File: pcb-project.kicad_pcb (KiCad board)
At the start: 2 copper layers, 110 x 60 mm, 62 parts, among them J1 Conn_01x03, J2 USB_C_Receptacle_USB2.0_16P, J3 Conn_01x14, J4 Conn_01x02, J5 Conn_01x05, J6 Conn_01x06, Q1 MMBT2222A, SW1 SW_Push, SW10 SW_Push, SW2 SW_Push, SW3 SW_Push, SW4 SW_Push, SW5 SW_Push, SW6 SW_Push, SW7 SW_Push, SW8 SW_Push, SW9 SW_Push, U1 RP2040, U2 W25Q128JVS, U3 AP2112K-3.3, U4 PAM8302AAD, Y1 12MHz

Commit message: Started arranging components, will continue tomorrow
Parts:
- moved J4 79.5 mm to (196.0, 104.0), turned to 0 degrees
- moved C17 61.4 mm to (174.5, 56.5), turned to 90 degrees
- moved C20 59.2 mm to (190.5, 92.5), turned to 0 degrees
- moved J5 54.2 mm to (112.0, 62.0), turned to 0 degrees
- moved C16 53.9 mm to (166.5, 56.5), turned to 90 degrees
- moved U4 49.2 mm to (186.0, 98.0), turned to 0 degrees
- moved U3 47.5 mm to (170.5, 56.5), turned to 0 degrees
- moved C23 45.9 mm to (179.5, 100.0), turned to 0 degrees
- moved C22 45.2 mm to (176.0, 100.0), turned to 0 degrees
- moved U2 42.9 mm to (169.0, 72.0)
- moved R13 42.6 mm to (179.5, 96.0), turned to 0 degrees
- moved R11 42.2 mm to (176.0, 96.0), turned to 0 degrees
- moved R12 41.9 mm to (176.0, 98.0), turned to 0 degrees
- moved C19 37.3 mm to (186.0, 92.5), turned to 0 degrees
- moved C21 31.9 mm to (179.5, 98.0), turned to 0 degrees
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
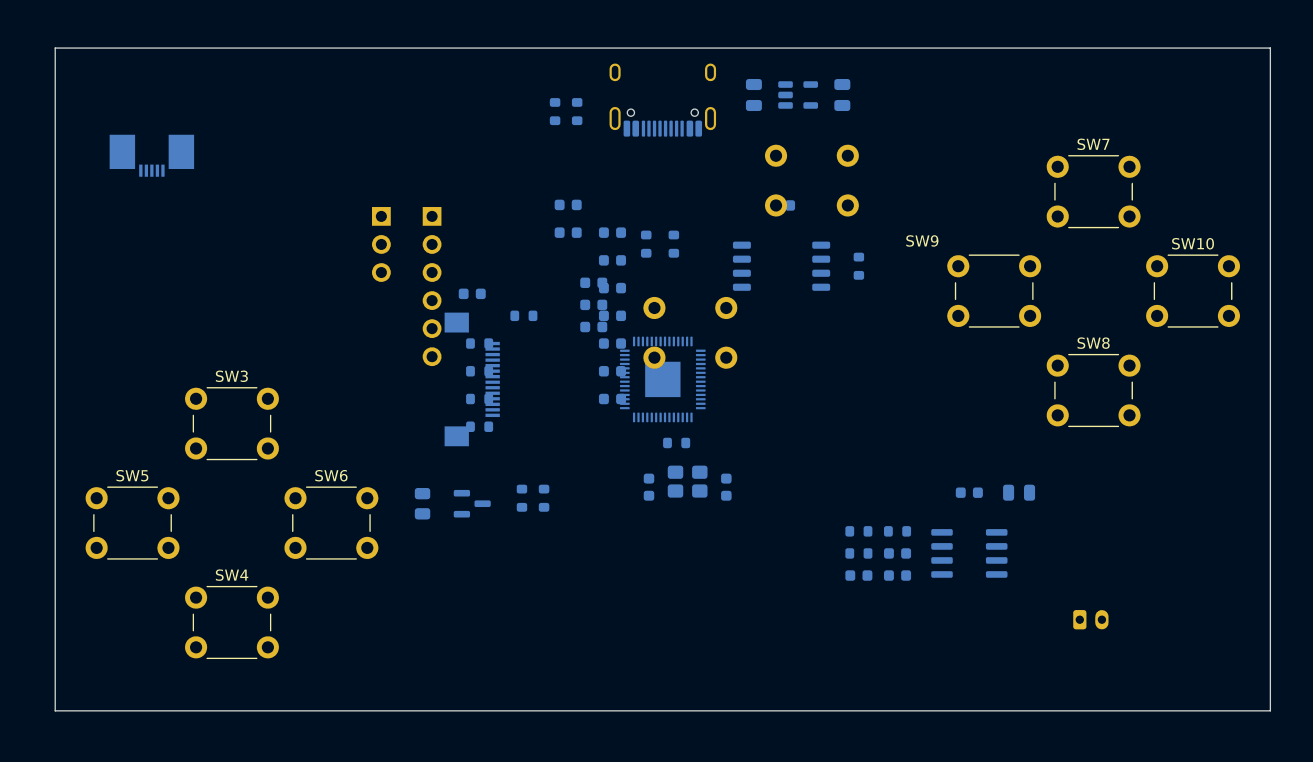
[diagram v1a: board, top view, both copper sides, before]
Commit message: Board outline and placement done
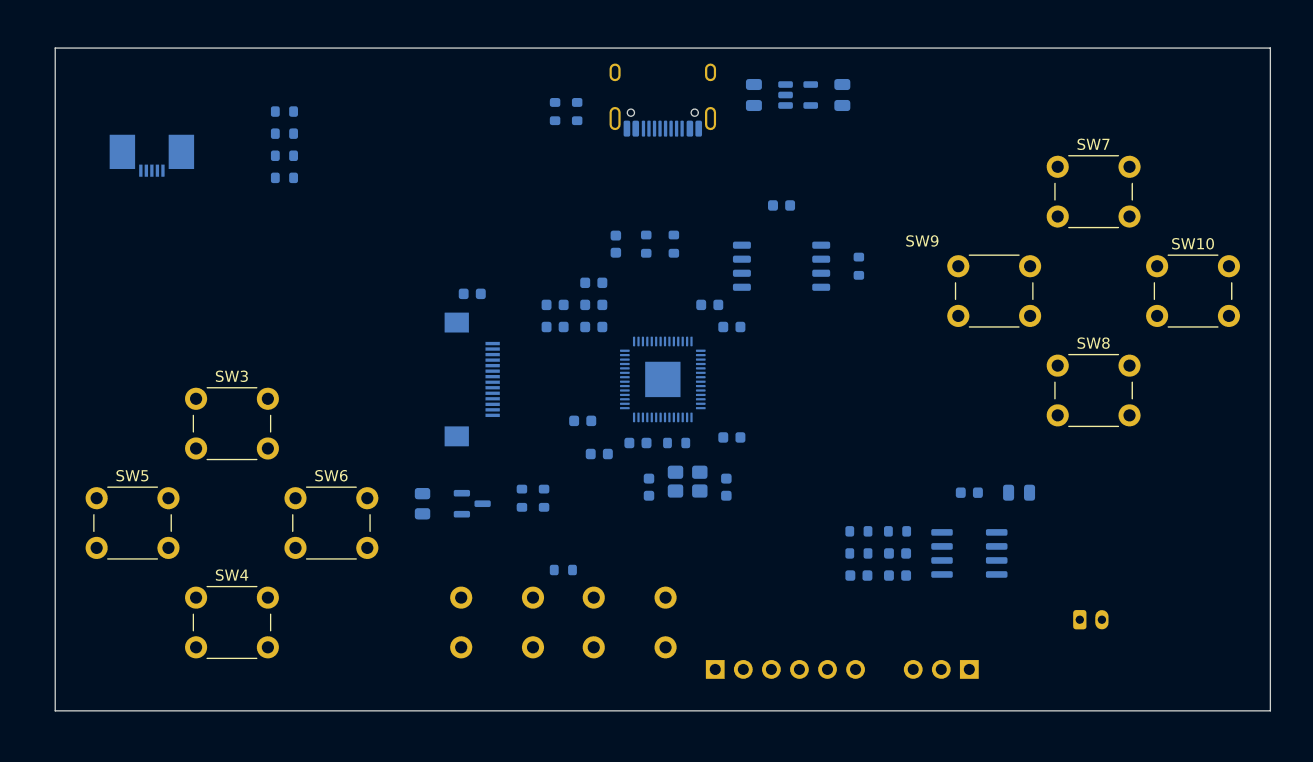
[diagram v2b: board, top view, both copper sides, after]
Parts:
- moved J1 67.2 mm to (186.0, 108.5), turned to 90 degrees
- moved SW1 56.6 mm to (140.0, 106.5), turned to 0 degrees
- moved J6 48.4 mm to (163.0, 108.5), turned to -90 degrees
- moved SW2 33.0 mm to (152.0, 106.5), turned to 0 degrees
- moved R18 28.6 mm to (124.0, 64.0), turned to 0 degrees
- moved R17 28.2 mm to (124.0, 62.0), turned to 0 degrees
- moved R15 27.8 mm to (124.0, 60.0), turned to 0 degrees
- moved R14 27.4 mm to (124.0, 58.0), turned to 0 degrees
- moved R3 23.3 mm to (149.2, 99.5), turned to 0 degrees
- moved C11 20.2 mm to (152.5, 89.0), turned to 0 degrees
- moved C4 17.3 mm to (164.5, 87.5), turned to 0 degrees
- moved C10 15.7 mm to (162.5, 75.5), turned to 0 degrees
- moved C2 13.8 mm to (164.5, 77.5), turned to 0 degrees
- moved C5 11.7 mm to (156.0, 88.0), turned to 0 degrees
- moved C8 9.98 mm to (148.5, 75.5), turned to 0 degrees
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
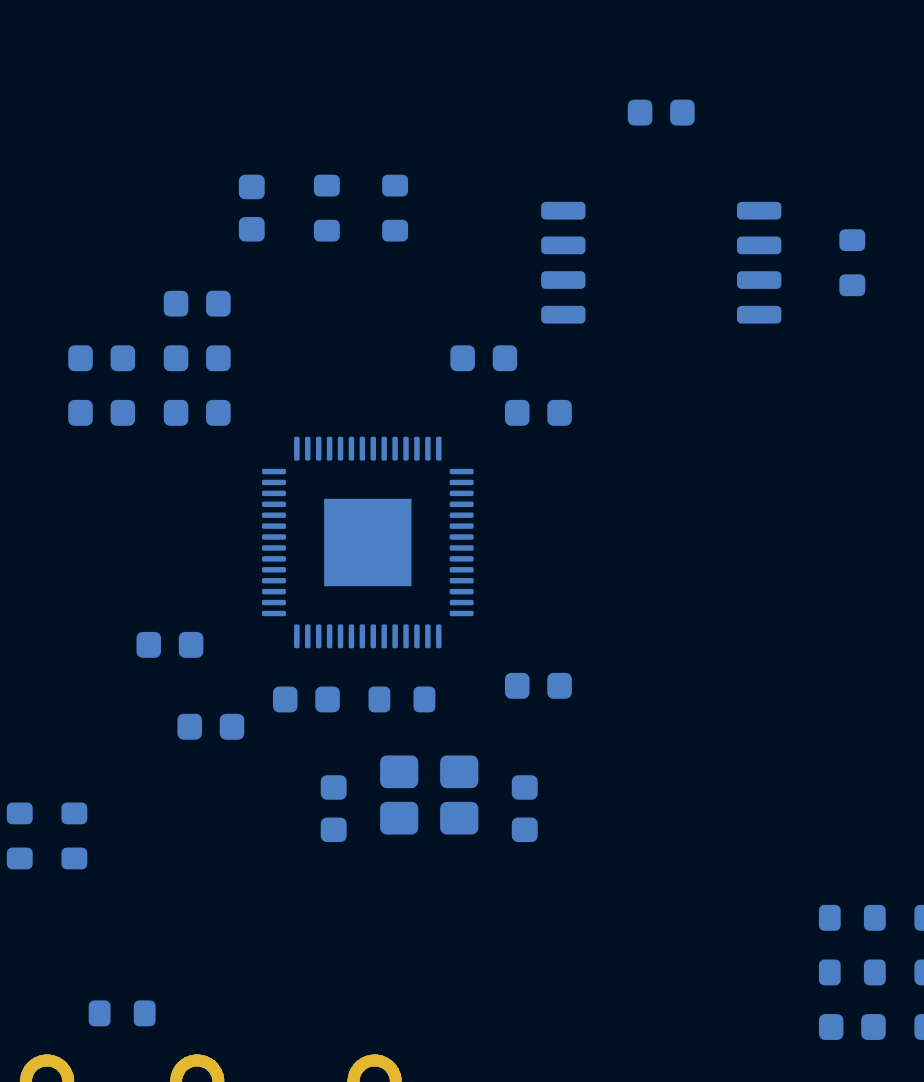
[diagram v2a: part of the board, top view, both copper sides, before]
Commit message: Crystal routed, RP2040 orientation fixed
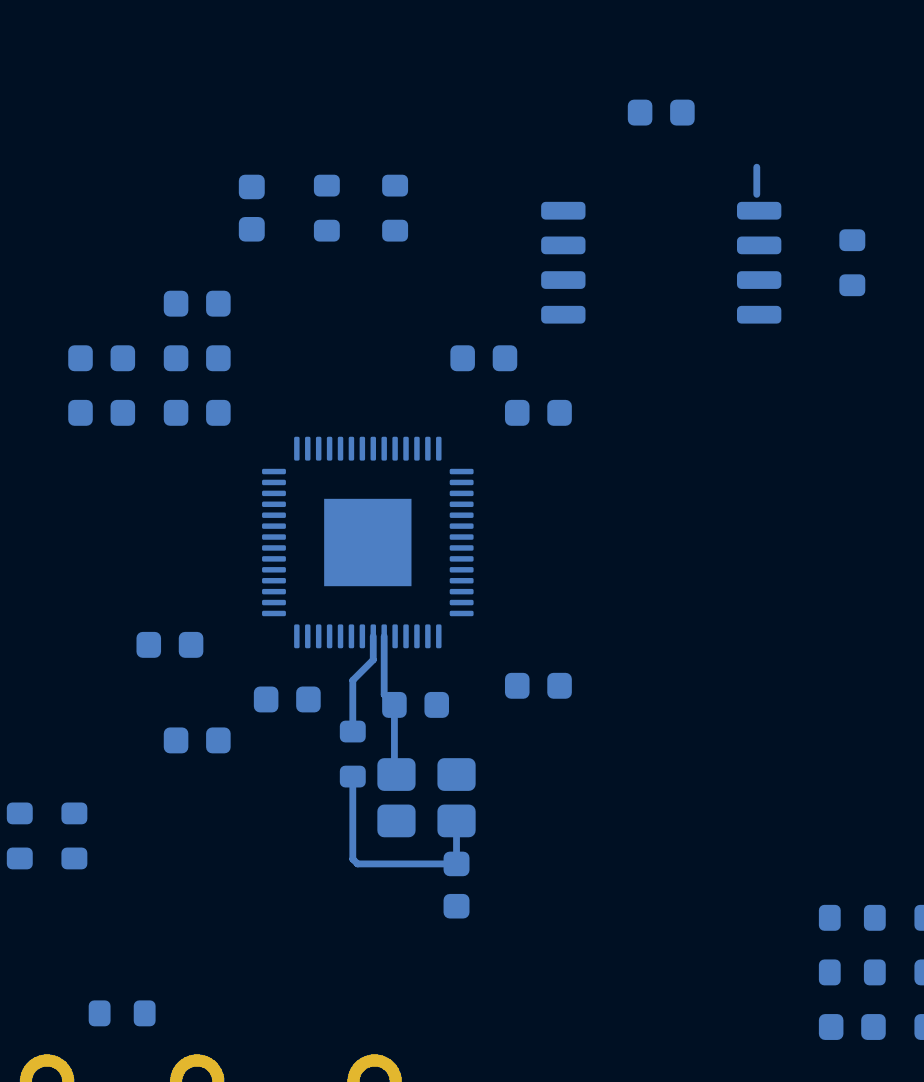
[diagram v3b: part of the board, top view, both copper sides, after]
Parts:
- moved C14 5.52 mm to (160.0, 88.2), turned to 0 degrees
- moved C13 5.30 mm to (161.5, 94.8), turned to -90 degrees
- moved R1 2.69 mm to (157.7, 90.0), turned to -90 degrees
- moved C11 0.71 mm to (152.0, 89.5)
- moved C5 0.70 mm to (155.3, 88.0)
- moved Y1 0.14 mm to (160.4, 91.6), turned to 0 degrees
- turned U1 to 180 degrees
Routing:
- net Net-(C13-Pad1): track 0.00 -> 8.47 mm
- net Net-(U1-XIN): track 0.00 -> 6.24 mm
- net Net-(U1-XOUT): track 0.00 -> 3.80 mm

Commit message: Crystal and USB hand-routed, before autoroute
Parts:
- turned R6 to -90 degrees
- turned R7 to -90 degrees
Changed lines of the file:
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@@
 	(footprint "Resistor_SMD:R_0603_1608Metric"
 		(layer "B.Cu")
-		(at 156.75 70 90)
+		(at 156.75 70 -90)
 		(descr "Resistor SMD 0603 (1608 Metric), square (rectangular) end terminal, IPC-7351 nominal, (Body size source: IPC-SM-782 page 72, https://www.pcb-3d.com/wordpress/wp-content/uploads/ipc-sm-782a_amendment_1_and_2.pdf)")
 		(tags "resistor")
 		(property "Reference" "R6"
-			(at 0 1.43 90)
+			(at 0 1.43 270)
 			(layer "B.SilkS")
 			(effects
@@
 		)
 		(property "Value" "27"
-			(at 0 -1.43 90)
+			(at 0 -1.43 270)
 			(layer "B.Fab")
 			(effects
@@
 		)
 		(property "Datasheet" ""
-			(at 0 0 90)
+			(at 0 0 270)
 			(layer "B.Fab")
 			(hide yes)
@@
 		)
 		(property "Description" "Resistor"
-			(at 0 0 90)
+			(at 0 0 270)
 			(layer "B.Fab")
 			(hide yes)
@@
 		)
 		(property "KiLib_Generator" "SMD_2terminal_chip_molded"
-			(at 0 0 90)
+			(at 0 0 270)
 			(layer "B.SilkS")
 			(hide yes)
@@
 		(duplicate_pad_numbers_are_jumpers no)
 		(fp_line
-			(start -0.237258 -0.5225)
-			(end 0.237258 -0.5225)
+			(start -0.237258 0.5225)
+			(end 0.237258 0.5225)
 			(stroke
 				(width 0.12)
@@
 		)
 		(fp_line
-			(start -0.237258 0.5225)
-			(end 0.237258 0.5225)
+			(start -0.237258 -0.5225)
+			(end 0.237258 -0.5225)
 			(stroke
 				(width 0.12)
@@
 		)
 		(fp_text user "${REFERENCE}"
-			(at 0 0 90)
+			(at 0 0 270)
 			(layer "B.Fab")
 			(effects
@@
 		)
 		(pad "1" smd roundrect
-			(at -0.825 0 90)
+			(at -0.825 0 270)
 			(size 0.8 0.95)
 			(layers "B.Cu" "B.Mask" "B.Paste")
@@
 		)
 		(pad "2" smd roundrect
-			(at 0.825 0 90)
+			(at 0.825 0 270)
 			(size 0.8 0.95)
 			(layers "B.Cu" "B.Mask" "B.Paste")
@@
 	(footprint "Resistor_SMD:R_0603_1608Metric"
 		(layer "B.Cu")
-		(at 159.25 70 90)
+		(at 159.25 70 -90)
 		(descr "Resistor SMD 0603 (1608 Metric), square (rectangular) end terminal, IPC-7351 nominal, (Body size source: IPC-SM-782 page 72, https://www.pcb-3d.com/wordpress/wp-content/uploads/ipc-sm-782a_amendment_1_and_2.pdf)")
 		(tags "resistor")
 		(property "Reference" "R7"
-			(at 0 1.43 90)
+			(at 0 1.43 270)
 			(layer "B.SilkS")
 			(effects
@@
 		)
 		(property "Value" "27"
-			(at 0 -1.43 90)
+			(at 0 -1.43 270)
 			(layer "B.Fab")
 			(effects
@@
 		)
 		(property "Datasheet" ""
-			(at 0 0 90)
+			(at 0 0 270)
 			(layer "B.Fab")
 			(hide yes)
@@
 		)
 		(property "Description" "Resistor"
-			(at 0 0 90)
+			(at 0 0 270)
 			(layer "B.Fab")
 			(hide yes)
@@
 		)
 		(property "KiLib_Generator" "SMD_2terminal_chip_molded"
-			(at 0 0 90)
+			(at 0 0 270)
 			(layer "B.SilkS")
 			(hide yes)
@@
 		(duplicate_pad_numbers_are_jumpers no)
 		(fp_line
-			(start -0.237258 -0.5225)
-			(end 0.237258 -0.5225)
+			(start -0.237258 0.5225)
+			(end 0.237258 0.5225)
 			(stroke
 				(width 0.12)
@@
 		)
 		(fp_line
-			(start -0.237258 0.5225)
-			(end 0.237258 0.5225)
+			(start -0.237258 -0.5225)
+			(end 0.237258 -0.5225)
 			(stroke
 				(width 0.12)
@@
 		)
 		(fp_text user "${REFERENCE}"
-			(at 0 0 90)
+			(at 0 0 270)
 			(layer "B.Fab")
 			(effects
@@
 		)
 		(pad "1" smd roundrect
-			(at -0.825 0 90)
+			(at -0.825 0 270)
 			(size 0.8 0.95)
 			(layers "B.Cu" "B.Mask" "B.Paste")
@@
 		)
 		(pad "2" smd roundrect
-			(at 0.825 0 90)
+			(at 0.825 0 270)
 			(size 0.8 0.95)
 			(layers "B.Cu" "B.Mask" "B.Paste")

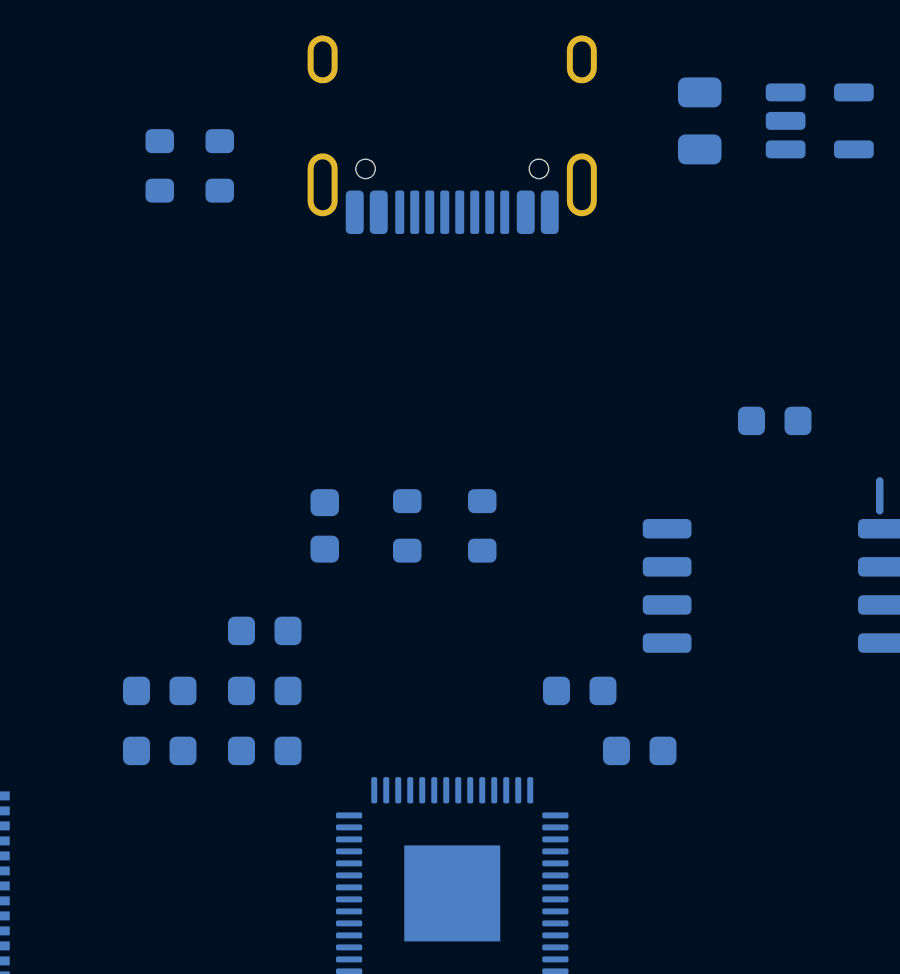
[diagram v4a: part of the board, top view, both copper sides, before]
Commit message: Cutouts added, hand-routed traces locked
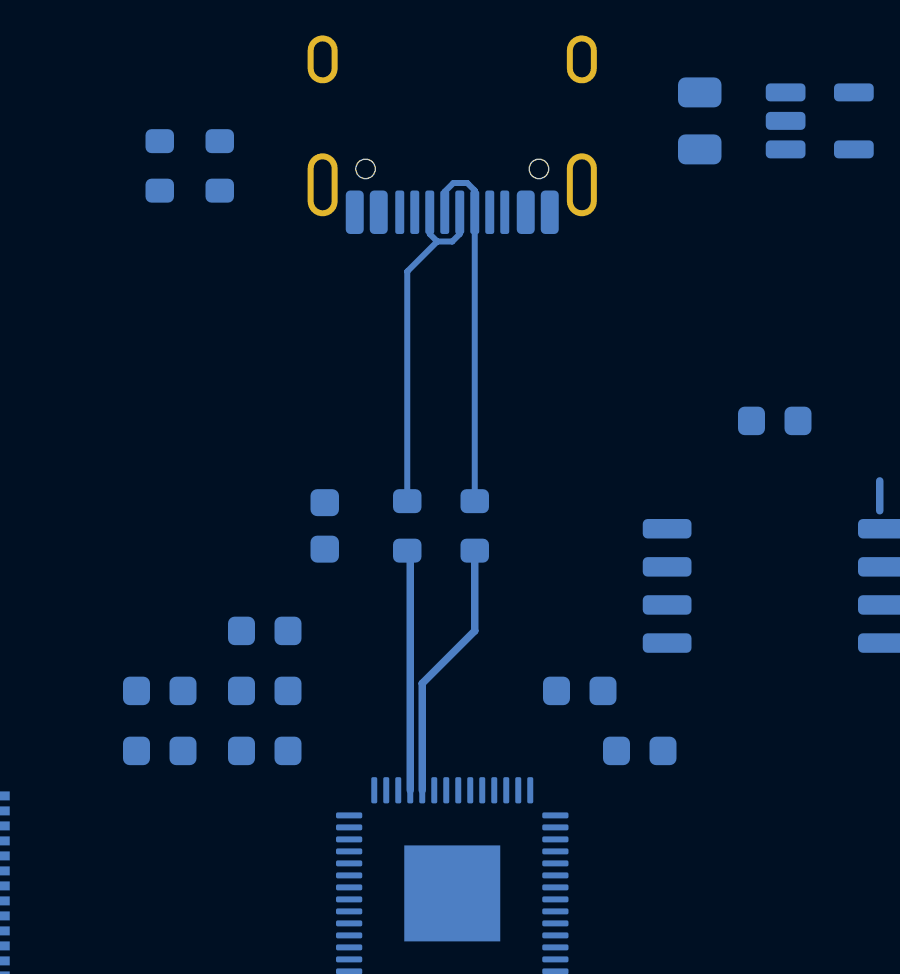
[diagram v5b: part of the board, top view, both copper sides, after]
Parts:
- moved R7 2.50 mm to (156.8, 70.0)
- moved R6 2.25 mm to (159.0, 70.0)
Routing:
- net /USB_D+: track 0.00 -> 12.3 mm
- net /USB_D-: track 0.00 -> 11.7 mm
- net Net-(U1-USB_DP): track 0.00 -> 8.71 mm
- net Net-(U1-USB_DM): track 0.00 -> 8.03 mm
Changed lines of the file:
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@@
 	(footprint "Resistor_SMD:R_0603_1608Metric"
 		(layer "B.Cu")
-		(at 156.75 70 -90)
+		(at 159 70 -90)
 		(descr "Resistor SMD 0603 (1608 Metric), square (rectangular) end terminal, IPC-7351 nominal, (Body size source: IPC-SM-782 page 72, https://www.pcb-3d.com/wordpress/wp-content/uploads/ipc-sm-782a_amendment_1_and_2.pdf)")
 		(tags "resistor")
@@
 	(footprint "Resistor_SMD:R_0603_1608Metric"
 		(layer "B.Cu")
-		(at 159.25 70 -90)
+		(at 156.75 70 -90)
 		(descr "Resistor SMD 0603 (1608 Metric), square (rectangular) end terminal, IPC-7351 nominal, (Body size source: IPC-SM-782 page 72, https://www.pcb-3d.com/wordpress/wp-content/uploads/ipc-sm-782a_amendment_1_and_2.pdf)")
 		(tags "resistor")
@@
 	)
 	(segment
+		(start 159 59.545)
+		(end 159 69.175)
+		(width 0.2)
+		(locked yes)
+		(layer "B.Cu")
+		(net "/USB_D+")
+	)
+	(segment
+		(start 159 58.820001)
+		(end 159 59.545)
+		(width 0.2)
+		(locked yes)
+		(layer "B.Cu")
+		(net "/USB_D+")
+	)
+	(segment
+		(start 158.288302 58.57)
+		(end 158.749999 58.57)
+		(width 0.2)
+		(locked yes)
+		(layer "B.Cu")
+		(net "/USB_D+")
+	)
+	(segment
+		(start 158 58.858302)
+		(end 158.288302 58.57)
+		(width 0.2)
+		(locked yes)
+		(layer "B.Cu")
+		(net "/USB_D+")
+	)
+	(segment
+		(start 158 59.545)
+		(end 158 58.858302)
+		(width 0.2)
+		(locked yes)
+		(layer "B.Cu")
+		(net "/USB_D+")
+	)
+	(segment
+		(start 158.749999 58.57)
+		(end 159 58.820001)
+		(width 0.2)
+		(locked yes)
+		(layer "B.Cu")
+		(net "/USB_D+")
+	)
+	(segment
+		(start 157.750001 60.52)
+		(end 158.249999 60.52)
+		(width 0.2)
+		(locked yes)
+		(layer "B.Cu")
+		(net "/USB_D-")
+	)
+	(segment
+		(start 157.750001 60.52)
+		(end 156.75 61.520001)
+		(width 0.2)
+		(locked yes)
+		(layer "B.Cu")
+		(net "/USB_D-")
+	)
+	(segment
+		(start 157.5 59.545)
+		(end 157.5 60.269999)
+		(width 0.2)
+		(locked yes)
+		(layer "B.Cu")
+		(net "/USB_D-")
+	)
+	(segment
+		(start 157.5 60.269999)
+		(end 157.750001 60.52)
+		(width 0.2)
+		(locked yes)
+		(layer "B.Cu")
+		(net "/USB_D-")
+	)
+	(segment
+		(start 158.5 60.269999)
+		(end 158.5 59.545)
+		(width 0.2)
+		(locked yes)
+		(layer "B.Cu")
+		(net "/USB_D-")
+	)
+	(segment
+		(start 156.75 61.520001)
+		(end 156.75 69.175)
+		(width 0.2)
+		(locked yes)
+		(layer "B.Cu")
+		(net "/USB_D-")
+	)
+	(segment
+		(start 158.249999 60.52)
+		(end 158.5 60.269999)
+		(width 0.2)
+		(locked yes)
+		(layer "B.Cu")
+		(net "/USB_D-")
+	)
+	(segment
 		(start 157.7 87.3)
 		(end 157.7 89.175)
 		(width 0.25)
+		(locked yes)
 		(layer "B.Cu")
 		(net "Net-(U1-XOUT)")
@@
 		(end 158.45 86.55)
 		(width 0.25)
+		(locked yes)
 		(layer "B.Cu")
 		(net "Net-(U1-XOUT)")
@@
 		(end 157.7 87.3)
 		(width 0.25)
+		(locked yes)
 		(layer "B.Cu")
 		(net "Net-(U1-XOUT)")
@@
 		(end 157.7 93.85)
 		(width 0.25)
+		(locked yes)
 		(layer "B.Cu")
 		(net "Net-(C13-Pad1)")
@@
 		(end 161.5 92.45)
 		(width 0.25)
+		(locked yes)
 		(layer "B.Cu")
 		(net "Net-(C13-Pad1)")
@@
 		(end 157.875 94.025)
 		(width 0.25)
+		(locked yes)
 		(layer "B.Cu")
 		(net "Net-(C13-Pad1)")
@@
 		(end 161.5 94.025)
 		(width 0.25)
+		(locked yes)
 		(layer "B.Cu")
 		(net "Net-(C13-Pad1)")
@@
 		(end 159.225 90.675)
 		(width 0.25)
+		(locked yes)
 		(layer "B.Cu")
 		(net "Net-(U1-XIN)")
@@
 		(end 159.3 90.75)
 		(width 0.25)
+		(locked yes)
 		(layer "B.Cu")
 		(net "Net-(U1-XIN)")
@@
 		(end 158.85 87.825)
 		(width 0.25)
+		(locked yes)
 		(layer "B.Cu")
 		(net "Net-(U1-XIN)")
@@
 		(end 172.5 69.495)
 		(width 0.25)
+		(locked yes)
 		(layer "B.Cu")
 		(net "Net-(U1-XIN)")
@@
 		(end 159.225 88.2)
 		(width 0.25)
+		(locked yes)
 		(layer "B.Cu")
 		(net "Net-(U1-XIN)")
 	)
+	(segment
+		(start 156.75 70.825)
+		(end 156.85 70.925)
+		(width 0.25)
+		(locked yes)
+		(layer "B.Cu")
+		(net "Net-(U1-USB_DM)")
+	)
+	(segment
+		(start 156.85 70.925)
+		(end 156.85 78.8125)
+		(width 0.25)
+		(locked yes)
+		(layer "B.Cu")
+		(net "Net-(U1-USB_DM)")
+	)
+	(segment
+		(start 157.25 75.25)
+		(end 157.25 78.8125)
+		(width 0.25)
+		(locked yes)
+		(layer "B.Cu")
+		(net "Net-(U1-USB_DP)")
+	)
+	(segment
+		(start 159 73.5)
+		(end 157.25 75.25)
+		(width 0.25)
+		(locked yes)
+		(layer "B.Cu")
+		(net "Net-(U1-USB_DP)")
+	)
+	(segment
+		(start 159 70.825)
+		(end 159 73.5)
+		(width 0.25)
+		(locked yes)
+		(layer "B.Cu")
+		(net "Net-(U1-USB_DP)")
+	)
 	(embedded_fonts no)
